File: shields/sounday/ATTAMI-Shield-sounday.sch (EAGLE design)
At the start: 18 parts, among them IC1 TP4056

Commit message: changes to cap and inductor
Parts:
- removed L2: 470μ, microbuilder:INDUCTOR0805
- added C3: 470u, dp_devices:CAPACITOR_POL-CASE_A
- L1: value 100μ -> 100µH
- R1, R2: device SparkFun-Passives:RESISTOR0805-RES -> dp_devices:RESISTOR-0603
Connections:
- new net N$8: L1.1, R3.2, SPKR.2
- net GND: now also C3.-; no longer L2.1
- net PB1: now also R3.1
- net PB4: now also L1.2; no longer SPKR.2
- net VCC: now also C3.+; no longer L2.2
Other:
- note added: "HI_QULITY mono"
- moved on the sheet: C4, L1, R3
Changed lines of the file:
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@@
 <part name="GND2" library="SparkFun" deviceset="GND" device=""/>
 <part name="C1" library="SparkFun-Capacitors" deviceset="10UF-6.3V-20%(1206)" device="" value="10uF"/>
-<part name="R1" library="SparkFun-Passives" deviceset="RESISTOR" device="0805-RES" value="1K"/>
-<part name="R2" library="SparkFun-Passives" deviceset="RESISTOR" device="0805-RES" value="1K"/>
+<part name="R1" library="dp_devices" deviceset="RESISTOR" device="-0603" value="1K"/>
+<part name="R2" library="dp_devices" deviceset="RESISTOR" device="-0603" value="1K"/>
 <part name="LED_CHARGIN" library="microbuilder" deviceset="LED" device="0805_NOOUTLINE"/>
 <part name="LED_READY" library="microbuilder" deviceset="LED" device="0805_NOOUTLINE"/>
@@
 <part name="SPKR" library="microbuilder" deviceset="HEADER-1X2" device="ROUND"/>
 <part name="GND3" library="SparkFun" deviceset="GND" device=""/>
-<part name="L1" library="microbuilder" deviceset="INDUCTOR" device="0805" value="100μ"/>
-<part name="L2" library="microbuilder" deviceset="INDUCTOR" device="0805" value="470μ"/>
+<part name="L1" library="microbuilder" deviceset="INDUCTOR" device="0805" value="100µH"/>
 <part name="C4" library="SparkFun-Capacitors" deviceset="0.1UF-25V(+80/-20%)(0603)" device="" value="0.1uF"/>
 <part name="R3" library="SparkFun-Passives" deviceset="RESISTOR" device="0805-RES" value="7K5"/>
+<part name="C3" library="dp_devices" deviceset="CAPACITOR_POL" device="-CASE_A" value="470u"/>
 </parts>
 <sheets>
@@
 <text x="52.324" y="164.592" size="1.778" layer="91">VCC (output)</text>
 <text x="10.414" y="164.592" size="1.778" layer="91">V_BAT (input)</text>
-<text x="76.2" y="93.98" size="1.778" layer="91">this should only be used when VBAT is
+<text x="73.66" y="109.22" size="1.778" layer="91">this should only be used when VBAT is
 connected to via USB plug 5V</text>
+<text x="144.78" y="111.76" size="1.778" layer="91">HI_QULITY mono</text>
 </plain>
 <instances>
@@
 <instance part="SPKR" gate="G$1" x="147.32" y="106.68" rot="R180"/>
 <instance part="GND3" gate="1" x="160.02" y="99.06"/>
-<instance part="L1" gate="G$1" x="177.8" y="101.6"/>
-<instance part="L2" gate="G$1" x="170.18" y="68.58" rot="R90"/>
-<instance part="C4" gate="G$1" x="157.48" y="68.58"/>
-<instance part="R3" gate="G$1" x="167.64" y="104.14" smashed="yes" rot="R90">
-<attribute name="NAME" x="166.1414" y="100.33" size="1.778" layer="95" rot="R90"/>
-<attribute name="VALUE" x="170.942" y="105.41" size="1.778" layer="96" rot="R90"/>
-</instance>
+<instance part="L1" gate="G$1" x="175.26" y="106.68"/>
+<instance part="C4" gate="G$1" x="149.86" y="68.58"/>
+<instance part="R3" gate="G$1" x="175.26" y="114.3" smashed="yes" rot="R180">
+<attribute name="NAME" x="179.07" y="112.8014" size="1.778" layer="95" rot="R180"/>
+<attribute name="VALUE" x="173.99" y="117.602" size="1.778" layer="96" rot="R180"/>
+</instance>
+<instance part="C3" gate="C" x="162.56" y="71.12"/>
 </instances>
 <busses>
@@
 <label x="182.88" y="66.04" size="1.778" layer="95"/>
 <pinref part="C4" gate="G$1" pin="2"/>
-<wire x1="157.48" y1="66.04" x2="157.48" y2="63.5" width="0.1524" layer="91"/>
-<pinref part="L2" gate="G$1" pin="1"/>
-<wire x1="157.48" y1="63.5" x2="170.18" y2="63.5" width="0.1524" layer="91"/>
-<wire x1="170.18" y1="63.5" x2="172.72" y2="63.5" width="0.1524" layer="91"/>
+<wire x1="149.86" y1="66.04" x2="149.86" y2="63.5" width="0.1524" layer="91"/>
+<wire x1="149.86" y1="63.5" x2="162.56" y2="63.5" width="0.1524" layer="91"/>
+<wire x1="162.56" y1="63.5" x2="172.72" y2="63.5" width="0.1524" layer="91"/>
 <wire x1="172.72" y1="63.5" x2="172.72" y2="66.04" width="0.1524" layer="91"/>
-<junction x="170.18" y="63.5"/>
 <wire x1="172.72" y1="66.04" x2="190.5" y2="66.04" width="0.1524" layer="91"/>
+<pinref part="C3" gate="C" pin="-"/>
+<wire x1="162.56" y1="66.04" x2="162.56" y2="63.5" width="0.1524" layer="91"/>
+<junction x="162.56" y="63.5"/>
 </segment>
 <segment>
@@
 <wire x1="190.5" y1="71.12" x2="172.72" y2="71.12" width="0.1524" layer="91"/>
 <wire x1="172.72" y1="71.12" x2="172.72" y2="73.66" width="0.1524" layer="91"/>
-<pinref part="L2" gate="G$1" pin="2"/>
-<wire x1="172.72" y1="73.66" x2="170.18" y2="73.66" width="0.1524" layer="91"/>
 <pinref part="C4" gate="G$1" pin="1"/>
-<wire x1="170.18" y1="73.66" x2="157.48" y2="73.66" width="0.1524" layer="91"/>
-<junction x="170.18" y="73.66"/>
+<wire x1="172.72" y1="73.66" x2="162.56" y2="73.66" width="0.1524" layer="91"/>
+<pinref part="C3" gate="C" pin="+"/>
+<wire x1="162.56" y1="73.66" x2="149.86" y2="73.66" width="0.1524" layer="91"/>
+<junction x="162.56" y="73.66"/>
 </segment>
 </net>
@@
 <label x="218.44" y="124.46" size="1.778" layer="95"/>
 </segment>
+<segment>
+<pinref part="R3" gate="G$1" pin="1"/>
+<wire x1="180.34" y1="114.3" x2="190.5" y2="114.3" width="0.1524" layer="91"/>
+<label x="185.42" y="114.3" size="1.778" layer="95"/>
+</segment>
 </net>
 <net name="PB2" class="0">
@@
 </segment>
 <segment>
-<pinref part="SPKR" gate="G$1" pin="2"/>
-<wire x1="149.86" y1="106.68" x2="157.48" y2="106.68" width="0.1524" layer="91"/>
-<label x="157.48" y="106.68" size="1.778" layer="95"/>
-<label x="157.48" y="106.68" size="1.778" layer="95"/>
+<pinref part="L1" gate="G$1" pin="2"/>
+<wire x1="180.34" y1="106.68" x2="190.5" y2="106.68" width="0.1524" layer="91"/>
+<label x="185.42" y="106.68" size="1.778" layer="95"/>
 </segment>
 </net>
@@
 </segment>
 </net>
+<net name="N$8" class="0">
+<segment>
+<pinref part="L1" gate="G$1" pin="1"/>
+<wire x1="149.86" y1="106.68" x2="167.64" y2="106.68" width="0.1524" layer="91"/>
+<wire x1="167.64" y1="106.68" x2="170.18" y2="106.68" width="0.1524" layer="91"/>
+<wire x1="167.64" y1="106.68" x2="167.64" y2="114.3" width="0.1524" layer="91"/>
+<junction x="167.64" y="106.68"/>
+<pinref part="R3" gate="G$1" pin="2"/>
+<wire x1="167.64" y1="114.3" x2="170.18" y2="114.3" width="0.1524" layer="91"/>
+<pinref part="SPKR" gate="G$1" pin="2"/>
+</segment>
+</net>

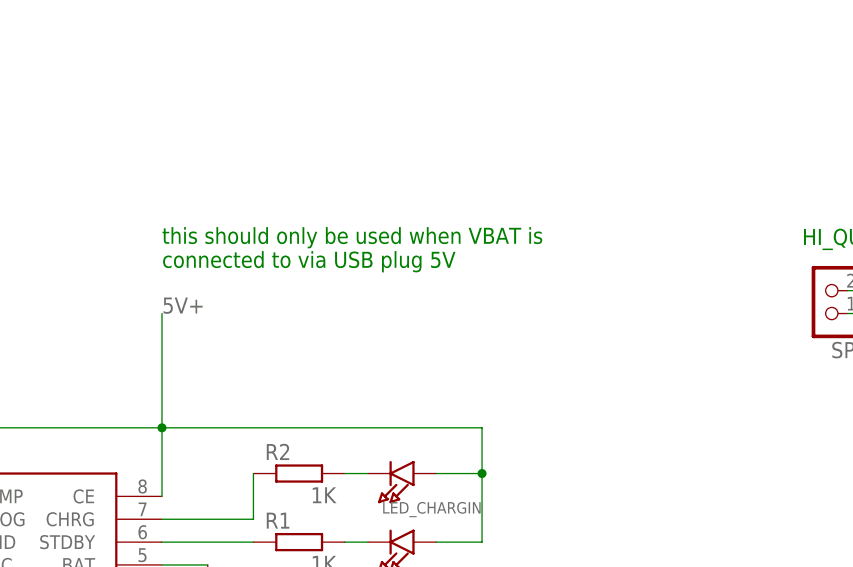
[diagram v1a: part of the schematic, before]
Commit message: V_BAT connect to charging circuit
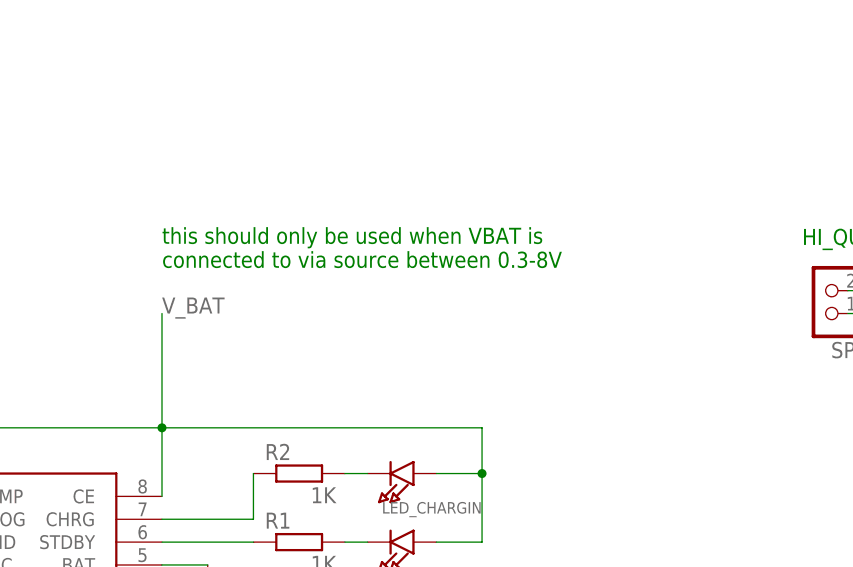
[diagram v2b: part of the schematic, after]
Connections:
- removed net 5V+: C2.1, IC1.CE, LED_CHARGIN.A, LED_READY.A
- net V_BAT: now also C2.1, IC1.CE, LED_CHARGIN.A, LED_READY.A
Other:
- note added: "this should only be used when VBAT is connected to via source between 0.3-8V"
- note removed: "this should only be used when VBAT is connected to via USB plug 5V"
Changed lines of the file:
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@@
 <text x="10.414" y="164.592" size="1.778" layer="91">V_BAT (input)</text>
 <text x="73.66" y="109.22" size="1.778" layer="91">this should only be used when VBAT is
-connected to via USB plug 5V</text>
+connected to via source between 0.3-8V</text>
 <text x="144.78" y="111.76" size="1.778" layer="91">HI_QULITY mono</text>
 </plain>
@@
 <label x="40.64" y="165.1" size="1.778" layer="95"/>
 </segment>
-</net>
-<net name="PB0" class="0">
-<segment>
-<pinref part="J1" gate="A" pin="2"/>
-<wire x1="231.14" y1="127" x2="218.44" y2="127" width="0.1524" layer="91"/>
-<label x="218.44" y="127" size="1.778" layer="95"/>
-</segment>
-<segment>
-<pinref part="U$4" gate="G$1" pin="DAT0"/>
-<wire x1="190.5" y1="63.5" x2="182.88" y2="63.5" width="0.1524" layer="91"/>
-<label x="182.88" y="63.5" size="1.778" layer="95"/>
-</segment>
-</net>
-<net name="PB1" class="0">
-<segment>
-<pinref part="J1" gate="A" pin="3"/>
-<wire x1="231.14" y1="124.46" x2="218.44" y2="124.46" width="0.1524" layer="91"/>
-<label x="218.44" y="124.46" size="1.778" layer="95"/>
-</segment>
-<segment>
-<pinref part="R3" gate="G$1" pin="1"/>
-<wire x1="180.34" y1="114.3" x2="190.5" y2="114.3" width="0.1524" layer="91"/>
-<label x="185.42" y="114.3" size="1.778" layer="95"/>
-</segment>
-</net>
-<net name="PB2" class="0">
-<segment>
-<pinref part="J1" gate="A" pin="4"/>
-<wire x1="231.14" y1="121.92" x2="218.44" y2="121.92" width="0.1524" layer="91"/>
-<label x="218.44" y="121.92" size="1.778" layer="95"/>
-</segment>
-<segment>
-<pinref part="U$4" gate="G$1" pin="CLK"/>
-<wire x1="190.5" y1="68.58" x2="182.88" y2="68.58" width="0.1524" layer="91"/>
-<label x="182.88" y="68.58" size="1.778" layer="95"/>
-</segment>
-</net>
-<net name="PB3" class="0">
-<segment>
-<pinref part="J1" gate="A" pin="5"/>
-<wire x1="218.44" y1="119.38" x2="231.14" y2="119.38" width="0.1524" layer="91"/>
-<label x="218.44" y="119.38" size="1.778" layer="95"/>
-</segment>
-<segment>
-<pinref part="U$4" gate="G$1" pin="DAT3"/>
-<wire x1="190.5" y1="76.2" x2="182.88" y2="76.2" width="0.1524" layer="91"/>
-<label x="182.88" y="76.2" size="1.778" layer="95"/>
-</segment>
-</net>
-<net name="PB4" class="0">
-<segment>
-<pinref part="J1" gate="A" pin="6"/>
-<wire x1="218.44" y1="116.84" x2="231.14" y2="116.84" width="0.1524" layer="91"/>
-<label x="218.44" y="116.84" size="1.778" layer="95"/>
-</segment>
-<segment>
-<pinref part="L1" gate="G$1" pin="2"/>
-<wire x1="180.34" y1="106.68" x2="190.5" y2="106.68" width="0.1524" layer="91"/>
-<label x="185.42" y="106.68" size="1.778" layer="95"/>
-</segment>
-</net>
-<net name="PB5" class="0">
-<segment>
-<pinref part="J1" gate="A" pin="7"/>
-<wire x1="218.44" y1="114.3" x2="231.14" y2="114.3" width="0.1524" layer="91"/>
-<label x="218.44" y="114.3" size="1.778" layer="95"/>
-</segment>
-<segment>
-<pinref part="U$4" gate="G$1" pin="CMD"/>
-<wire x1="190.5" y1="73.66" x2="182.88" y2="73.66" width="0.1524" layer="91"/>
-<label x="182.88" y="73.66" size="1.778" layer="95"/>
-</segment>
-</net>
-<net name="N$1" class="0">
-<segment>
-<pinref part="IC1" gate="G$1" pin="BAT"/>
-<pinref part="C1" gate="G$1" pin="1"/>
-<wire x1="73.66" y1="76.2" x2="78.74" y2="76.2" width="0.1524" layer="91"/>
-</segment>
-</net>
-<net name="N$3" class="0">
-<segment>
-<pinref part="LED_CHARGIN" gate="G$1" pin="C"/>
-<pinref part="R2" gate="G$1" pin="2"/>
-<wire x1="96.52" y1="86.36" x2="93.98" y2="86.36" width="0.1524" layer="91"/>
-</segment>
-</net>
-<net name="N$4" class="0">
-<segment>
-<pinref part="LED_READY" gate="G$1" pin="C"/>
-<pinref part="R1" gate="G$1" pin="2"/>
-<wire x1="96.52" y1="78.74" x2="93.98" y2="78.74" width="0.1524" layer="91"/>
-</segment>
-</net>
-<net name="N$5" class="0">
-<segment>
-<pinref part="R1" gate="G$1" pin="1"/>
-<pinref part="IC1" gate="G$1" pin="STDBY"/>
-<wire x1="83.82" y1="78.74" x2="73.66" y2="78.74" width="0.1524" layer="91"/>
-</segment>
-</net>
-<net name="N$6" class="0">
-<segment>
-<pinref part="R2" gate="G$1" pin="1"/>
-<wire x1="83.82" y1="86.36" x2="83.82" y2="81.28" width="0.1524" layer="91"/>
-<pinref part="IC1" gate="G$1" pin="CHRG"/>
-<wire x1="83.82" y1="81.28" x2="73.66" y2="81.28" width="0.1524" layer="91"/>
-</segment>
-</net>
-<net name="5V+" class="0">
 <segment>
 <pinref part="IC1" gate="G$1" pin="CE"/>
@@
 </segment>
 </net>
+<net name="PB0" class="0">
+<segment>
+<pinref part="J1" gate="A" pin="2"/>
+<wire x1="231.14" y1="127" x2="218.44" y2="127" width="0.1524" layer="91"/>
+<label x="218.44" y="127" size="1.778" layer="95"/>
+</segment>
+<segment>
+<pinref part="U$4" gate="G$1" pin="DAT0"/>
+<wire x1="190.5" y1="63.5" x2="182.88" y2="63.5" width="0.1524" layer="91"/>
+<label x="182.88" y="63.5" size="1.778" layer="95"/>
+</segment>
+</net>
+<net name="PB1" class="0">
+<segment>
+<pinref part="J1" gate="A" pin="3"/>
+<wire x1="231.14" y1="124.46" x2="218.44" y2="124.46" width="0.1524" layer="91"/>
+<label x="218.44" y="124.46" size="1.778" layer="95"/>
+</segment>
+<segment>
+<pinref part="R3" gate="G$1" pin="1"/>
+<wire x1="180.34" y1="114.3" x2="190.5" y2="114.3" width="0.1524" layer="91"/>
+<label x="185.42" y="114.3" size="1.778" layer="95"/>
+</segment>
+</net>
+<net name="PB2" class="0">
+<segment>
+<pinref part="J1" gate="A" pin="4"/>
+<wire x1="231.14" y1="121.92" x2="218.44" y2="121.92" width="0.1524" layer="91"/>
+<label x="218.44" y="121.92" size="1.778" layer="95"/>
+</segment>
+<segment>
+<pinref part="U$4" gate="G$1" pin="CLK"/>
+<wire x1="190.5" y1="68.58" x2="182.88" y2="68.58" width="0.1524" layer="91"/>
+<label x="182.88" y="68.58" size="1.778" layer="95"/>
+</segment>
+</net>
+<net name="PB3" class="0">
+<segment>
+<pinref part="J1" gate="A" pin="5"/>
+<wire x1="218.44" y1="119.38" x2="231.14" y2="119.38" width="0.1524" layer="91"/>
+<label x="218.44" y="119.38" size="1.778" layer="95"/>
+</segment>
+<segment>
+<pinref part="U$4" gate="G$1" pin="DAT3"/>
+<wire x1="190.5" y1="76.2" x2="182.88" y2="76.2" width="0.1524" layer="91"/>
+<label x="182.88" y="76.2" size="1.778" layer="95"/>
+</segment>
+</net>
+<net name="PB4" class="0">
+<segment>
+<pinref part="J1" gate="A" pin="6"/>
+<wire x1="218.44" y1="116.84" x2="231.14" y2="116.84" width="0.1524" layer="91"/>
+<label x="218.44" y="116.84" size="1.778" layer="95"/>
+</segment>
+<segment>
+<pinref part="L1" gate="G$1" pin="2"/>
+<wire x1="180.34" y1="106.68" x2="190.5" y2="106.68" width="0.1524" layer="91"/>
+<label x="185.42" y="106.68" size="1.778" layer="95"/>
+</segment>
+</net>
+<net name="PB5" class="0">
+<segment>
+<pinref part="J1" gate="A" pin="7"/>
+<wire x1="218.44" y1="114.3" x2="231.14" y2="114.3" width="0.1524" layer="91"/>
+<label x="218.44" y="114.3" size="1.778" layer="95"/>
+</segment>
+<segment>
+<pinref part="U$4" gate="G$1" pin="CMD"/>
+<wire x1="190.5" y1="73.66" x2="182.88" y2="73.66" width="0.1524" layer="91"/>
+<label x="182.88" y="73.66" size="1.778" layer="95"/>
+</segment>
+</net>
+<net name="N$1" class="0">
+<segment>
+<pinref part="IC1" gate="G$1" pin="BAT"/>
+<pinref part="C1" gate="G$1" pin="1"/>
+<wire x1="73.66" y1="76.2" x2="78.74" y2="76.2" width="0.1524" layer="91"/>
+</segment>
+</net>
+<net name="N$3" class="0">
+<segment>
+<pinref part="LED_CHARGIN" gate="G$1" pin="C"/>
+<pinref part="R2" gate="G$1" pin="2"/>
+<wire x1="96.52" y1="86.36" x2="93.98" y2="86.36" width="0.1524" layer="91"/>
+</segment>
+</net>
+<net name="N$4" class="0">
+<segment>
+<pinref part="LED_READY" gate="G$1" pin="C"/>
+<pinref part="R1" gate="G$1" pin="2"/>
+<wire x1="96.52" y1="78.74" x2="93.98" y2="78.74" width="0.1524" layer="91"/>
+</segment>
+</net>
+<net name="N$5" class="0">
+<segment>
+<pinref part="R1" gate="G$1" pin="1"/>
+<pinref part="IC1" gate="G$1" pin="STDBY"/>
+<wire x1="83.82" y1="78.74" x2="73.66" y2="78.74" width="0.1524" layer="91"/>
+</segment>
+</net>
+<net name="N$6" class="0">
+<segment>
+<pinref part="R2" gate="G$1" pin="1"/>
+<wire x1="83.82" y1="86.36" x2="83.82" y2="81.28" width="0.1524" layer="91"/>
+<pinref part="IC1" gate="G$1" pin="CHRG"/>
+<wire x1="83.82" y1="81.28" x2="73.66" y2="81.28" width="0.1524" layer="91"/>
+</segment>
+</net>
